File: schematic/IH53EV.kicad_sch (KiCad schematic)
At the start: 43 parts, among them K2 T9AP1D52-12, K3 Cole Hersee 24213, K4 G9EJ-1-E-UVD DC12, SW1 Kill Switch HVBD6AXR, SW3 Ignition Switch, SW4 Inertia Switch

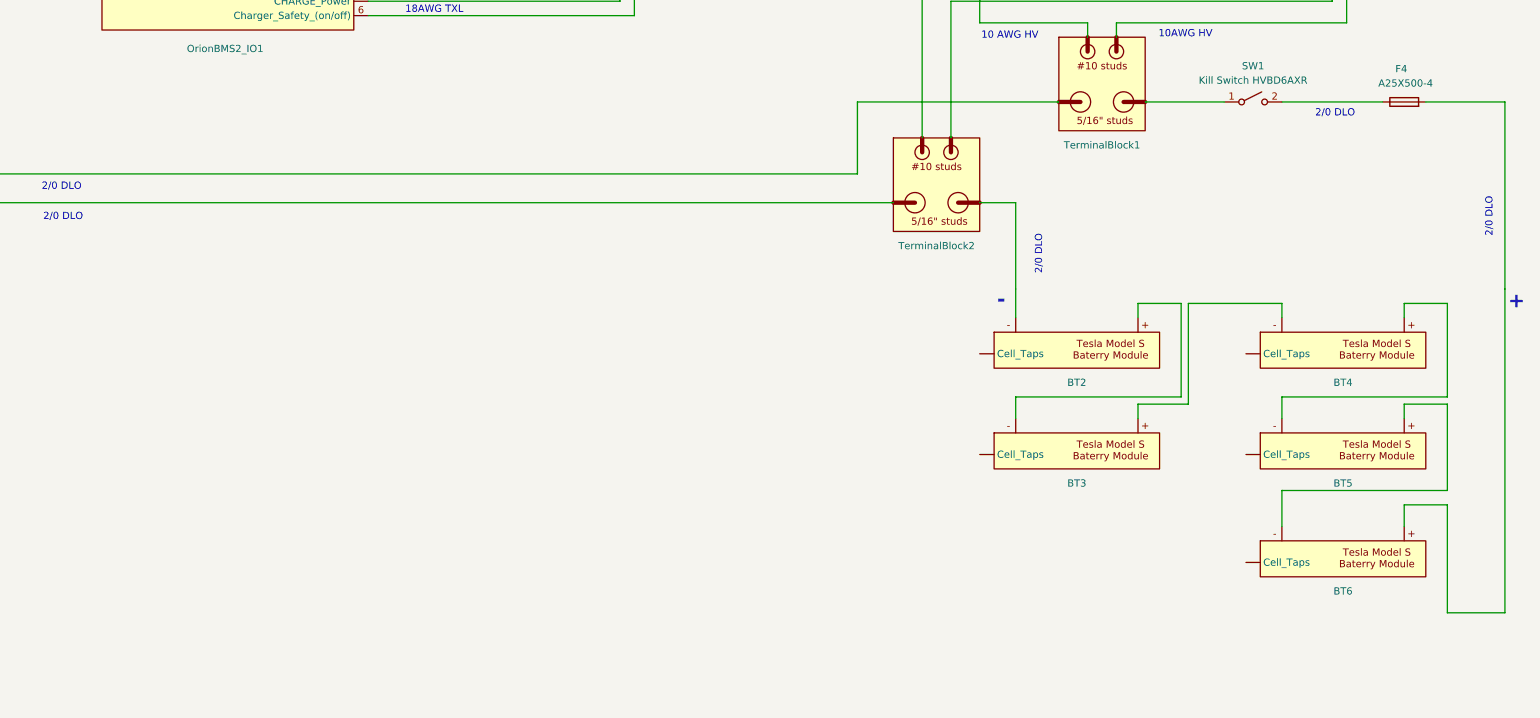
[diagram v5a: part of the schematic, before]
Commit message: add thru-wall terminals
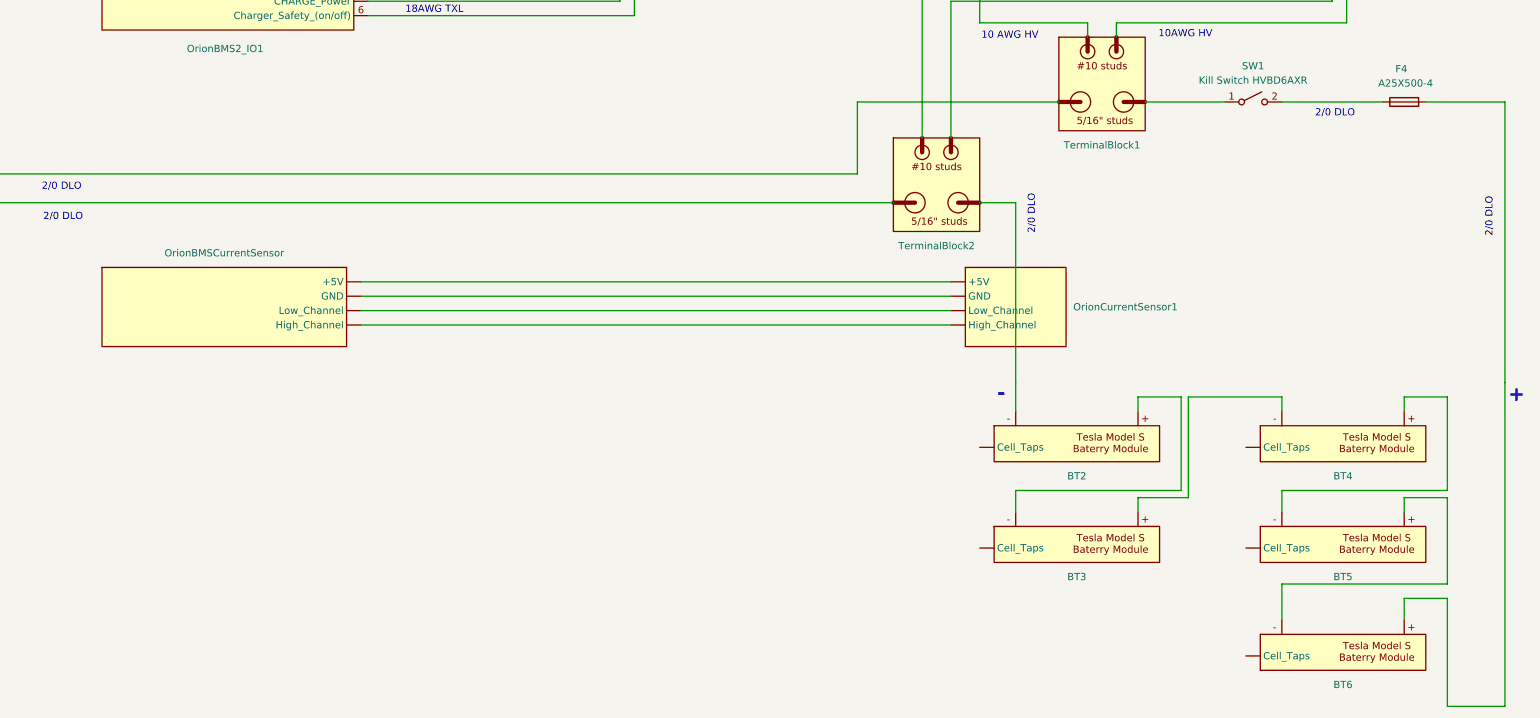
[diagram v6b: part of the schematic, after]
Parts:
- added OrionBMSCurrentSensor: (no value), symbol Orion_BMS:Current_Sensor
- added OrionCurrentSensor1: (no value), symbol Current Sensor:Orion_Current_Sensor
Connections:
- net at DeutschDTM3-pin1.: no longer BBCANOPCanbusIsolator1.
- net at DelphiWeather4Pack1.: now also OrionBMS2_IO1.7 (DISCHARGE_enable); no longer Blue_Sea_5032. (GND)
- net at Blue_Sea_5032.2: no longer DelphiWeather4Pack1.
- net at Blue_Sea_5032.5: now also SW4.2 (B)
- net at BT4.: now also BT3.
- net at BT5.: now also BT6.; no longer BT4.
- net at BT3.: no longer BT4.
- net at NON_ISOLATED_LOGIC_X1_CONTROLLER. (B+): now also G1.A2-; no longer Anderson350A600V1.
- net at BT2.: now also TerminalBlock2.
- net at TerminalBlock2.: now also 2Pole_1000V_DC_10Amp1.2 (B); no longer BT2.
- net at BT6.: no longer BT5.
- net at Anderson350A600V1.: now also TerminalBlock2.; no longer TerminalBlock3.
- net at TerminalBlock1.: now also Circuit_Breaker4.2 (B); no longer Anderson350A600V1.
- net at DCIS_DC/DC_Convertor1. (Key_Switch_Control): now also DJ7021-8-1.; no longer dj70310-6.3-1.
- net at dj70310-6.3-1.: now also 2Pole_1000V_DC_10Amp1.1 (A); no longer DCIS_DC/DC_Convertor1. (Key_Switch_Control)
- net at TerminalBlock3.: now also Circuit_Breaker2.2 (B)
- new net: BBCANOPCanbusIsolator1., DelphiWeather4Pack1., OrionBMS2_IO1.12 (Ground)
- new net: BBCANOPCanbusIsolator1., DeutschDTM3-pin1. (x2)
- new net: OrionBMSCurrentSensor. (High_Channel), OrionCurrentSensor1. (High_Channel) (x4)
- new net: Blue_Sea_5032. (GND), DelphiWeather4Pack1.
- new net: Blue_Sea_5032.2, DelphiWeather4Pack1.
- new net: Blue_Sea_5032.6 (Ready/Precharge), DelphiWeather4Pack1., K2.1
- new net: BT4., BT5.
- new net: Anderson350A600V1., NON_ISOLATED_LOGIC_X1_CONTROLLER. (B+)
- new net: BT2., BT3.
- new net: Anderson350A600V1., TerminalBlock3.
- new net: Anderson350A600V1., TerminalBlock1.
- new net: DCIS_DC/DC_Convertor1. (Key_Switch_Control), dj70310-6.3-1. (x3)
- new net: DCIS_DC/DC_Convertor1. (Key_Switch_Control), DJ7021-8-1.
- now unconnected: BT3., Blue_Sea_5032.6 (Ready/Precharge), DeutschDTM3-pin1.
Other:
- moved on the sheet: BT2, BT3, BT4, BT5, BT6

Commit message: add dashboard
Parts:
- added SW5: Instruments, symbol Switch:SW_SPST
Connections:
- net GND: now also K4.3; no longer K4.1
- net at DeutschDTM3-pin1.: no longer BBCANOPCanbusIsolator1.
- net at DelphiWeather4Pack1.: now also OrionBMS2_IO1.7 (DISCHARGE_enable); no longer Blue_Sea_5032. (GND)
- net at Blue_Sea_5032.2: no longer DelphiWeather4Pack1.
- net at Blue_Sea_5032.4: now also SW5.1 (A)
- net at Blue_Sea_5032.5: now also SW4.2 (B)
- net at BT4.: now also BT3.
- net at BT5.: now also BT6.; no longer BT4.
- net at BT3.: no longer BT4.
- net at NON_ISOLATED_LOGIC_X1_CONTROLLER. (B+): now also G1.A2-; no longer Anderson350A600V1.
- net at K4.4: now also BBCANOPCanbusIsolator1., DelphiWeather4Pack1., OrionBMS2_IO1.2 (READY_Power); no longer dj70310-6.3-1.
- net at BT2.: now also TerminalBlock2.
- net at TerminalBlock2.: now also 2Pole_1000V_DC_10Amp1.2 (B); no longer BT2.
- net at BT6.: no longer BT5.
- net at Anderson350A600V1.: now also TerminalBlock2.; no longer TerminalBlock3.
- net at TerminalBlock1.: now also Circuit_Breaker4.2 (B); no longer Anderson350A600V1.
- net at DCIS_DC/DC_Convertor1. (Key_Switch_Control): now also DJ7021-8-1.; no longer dj70310-6.3-1.
- net at dj70310-6.3-1.: now also 2Pole_1000V_DC_10Amp1.1 (A); no longer DCIS_DC/DC_Convertor1. (Key_Switch_Control)
- net at TerminalBlock3.: now also Circuit_Breaker2.2 (B)
- new net: BBCANOPCanbusIsolator1., DelphiWeather4Pack1., OrionBMS2_IO1.12 (Ground)
- new net: BBCANOPCanbusIsolator1., DeutschDTM3-pin1. (x2)
- new net: OrionBMSCurrentSensor. (High_Channel), OrionCurrentSensor1. (High_Channel) (x3)
- new net: Blue_Sea_5032. (GND), DelphiWeather4Pack1.
- new net: Blue_Sea_5032.2, DelphiWeather4Pack1.
- new net: Blue_Sea_5032.6 (Ready/Precharge), DelphiWeather4Pack1., K2.1
- new net: BT4., BT5.
- new net: Anderson350A600V1., NON_ISOLATED_LOGIC_X1_CONTROLLER. (B+)
- new net: Circuit_Breaker4.1 (A), K4.1, dj70310-6.3-1.
- new net: K4.2, dj70310-6.3-1.
- new net: BT2., BT3.
- new net: Anderson350A600V1., TerminalBlock3.
- new net: Anderson350A600V1., TerminalBlock1.
- new net: DCIS_DC/DC_Convertor1. (Key_Switch_Control), dj70310-6.3-1. (x3)
- new net: DCIS_DC/DC_Convertor1. (Key_Switch_Control), DJ7021-8-1.
- now unconnected: BT3., Blue_Sea_5032.6 (Ready/Precharge), DeutschDTM3-pin1.
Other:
- note added: "to PiCAN 3 +12V (SMPS feeds Pi + TD2)"
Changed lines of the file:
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@@
 	(title_block
 		(title "1953 International EV Conversion")
-		(date "2026-08-24")
+		(date "2026-09-07")
+	)
+	(wire
+		(pts
+			(xy 275.59 218.44) (xy 290.83 218.44)
+		)
+		(stroke
+			(width 0)
+			(type default)
+			(color 0 0 255 1)
+		)
+	)
+	(wire
+		(pts
+			(xy 187.96 125.73) (xy 205.74 125.73)
+		)
+		(stroke
+			(width 0)
+			(type default)
+		)
+	)
+	(wire
+		(pts
+			(xy 215.9 125.73) (xy 233.68 125.73)
+		)
+		(stroke
+			(width 0)
+			(type default)
+		)
+	)
+	(text "to PiCAN 3 +12V\n(SMPS feeds Pi + TD2)"
+		(exclude_from_sim no)
+		(at 248.92 125.73 0)
+		(effects
+			(font
+				(size 1.27 1.27)
+			)
+		)
+	)
+	(text "18AWG TXL"
+		(exclude_from_sim no)
+		(at 196.85 122.0 0)
+		(effects
+			(font
+				(size 1.27 1.27)
+			)
+		)
 	)
 	(text "18AWG TXL"
@@
 	(wire
 		(pts
-			(xy 275.59 218.44) (xy 290.83 218.44)
-		)
-		(stroke
-			(width 0)
-			(type default)
-			(color 0 0 255 1)
-		)
-	)
-	(wire
-		(pts
 			(xy 457.2 151.13) (xy 457.2 77.47)
 		)
@@
 	)
 	(symbol
+		(lib_id "Switch:SW_SPST")
+		(at 210.82 125.73 0)
+		(unit 1)
+		(body_style 1)
+		(exclude_from_sim no)
+		(in_bom yes)
+		(on_board yes)
+		(in_pos_files yes)
+		(dnp no)
+		(fields_autoplaced yes)
+		(property "Reference" "SW5"
+			(at 210.82 118.11 0)
+			(show_name no)
+			(do_not_autoplace no)
+			(effects
+				(font
+					(size 1.27 1.27)
+				)
+			)
+		)
+		(property "Value" "Instruments"
+			(at 210.82 120.65 0)
+			(show_name no)
+			(do_not_autoplace no)
+			(effects
+				(font
+					(size 1.27 1.27)
+				)
+			)
+		)
+		(property "Footprint" ""
+			(at 210.82 125.73 0)
+			(hide yes)
+			(show_name no)
+			(do_not_autoplace no)
+			(effects
+				(font
+					(size 1.27 1.27)
+				)
+			)
+		)
+		(property "Datasheet" ""
+			(at 210.82 125.73 0)
+			(hide yes)
+			(show_name no)
+			(do_not_autoplace no)
+			(effects
+				(font
+					(size 1.27 1.27)
+				)
+			)
+		)
+		(property "Description" "Single Pole Single Throw (SPST) switch"
+			(at 210.82 125.73 0)
+			(hide yes)
+			(show_name no)
+			(do_not_autoplace no)
+			(effects
+				(font
+					(size 1.27 1.27)
+				)
+			)
+		)
+		(pin "1"
+		)
+		(pin "2"
+		)
+		(instances
+			(project "IH53EV"
+				(path "/20bcdb30-6107-4dbd-a268-7abc52ed82ed"
+					(reference "SW5")
+					(unit 1)
+				)
+			)
+		)
+	)
+	(symbol
 		(lib_id "Device:Fuse")
 		(at 90.17 105.41 180)
@@
 	)
 	(symbol
+		(lib_name "Relay_SPST-NO_2")
 		(lib_id "Relay:Relay_SPST-NO")
 		(at 285.75 95.25 90)

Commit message: update bus bar
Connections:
- net at DeutschDTM3-pin1.: no longer BBCANOPCanbusIsolator1.
- net at DelphiWeather4Pack1.: now also OrionBMS2_IO1.7 (DISCHARGE_enable); no longer Blue_Sea_5032. (GND)
- net at Blue_Sea_5032.2: no longer DelphiWeather4Pack1.
- net at Blue_Sea_5032.4: now also SW5.1 (A)
- net at Blue_Sea_5032.5: now also SW4.2 (B)
- net at BT4.: now also BT3.
- net at BT5.: now also BT6.; no longer BT4.
- net at BT3.: no longer BT4.
- net at NON_ISOLATED_LOGIC_X1_CONTROLLER. (B+): now also G1.A2-; no longer Anderson350A600V1.
- net at BT2.: now also TerminalBlock2.
- net at TerminalBlock2.: now also 2Pole_1000V_DC_10Amp1.2 (B); no longer BT2.
- net at BT6.: no longer BT5.
- net at Anderson350A600V1.: now also TerminalBlock2.; no longer TerminalBlock3.
- net at TerminalBlock1.: now also Circuit_Breaker4.2 (B); no longer Anderson350A600V1.
- net at DCIS_DC/DC_Convertor1. (Key_Switch_Control): now also DJ7021-8-1.; no longer dj70310-6.3-1.
- net at dj70310-6.3-1.: now also 2Pole_1000V_DC_10Amp1.1 (A); no longer DCIS_DC/DC_Convertor1. (Key_Switch_Control)
- net at TerminalBlock3.: now also Circuit_Breaker2.2 (B)
- new net: BBCANOPCanbusIsolator1., DelphiWeather4Pack1., OrionBMS2_IO1.12 (Ground)
- new net: BBCANOPCanbusIsolator1., DeutschDTM3-pin1. (x2)
- new net: OrionBMSCurrentSensor. (High_Channel), OrionCurrentSensor1. (High_Channel) (x3)
- new net: Blue_Sea_5032. (GND), DelphiWeather4Pack1.
- new net: Blue_Sea_5032.2, DelphiWeather4Pack1.
- new net: Blue_Sea_5032.6 (Ready/Precharge), DelphiWeather4Pack1., K2.1
- new net: BT4., BT5.
- new net: Anderson350A600V1., NON_ISOLATED_LOGIC_X1_CONTROLLER. (B+)
- new net: BT2., BT3.
- new net: Anderson350A600V1., TerminalBlock3.
- new net: Anderson350A600V1., TerminalBlock1.
- new net: DCIS_DC/DC_Convertor1. (Key_Switch_Control), dj70310-6.3-1. (x3)
- new net: DCIS_DC/DC_Convertor1. (Key_Switch_Control), DJ7021-8-1.
- now unconnected: BT3., Blue_Sea_5032.6 (Ready/Precharge), DeutschDTM3-pin1.
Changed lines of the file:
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@@
 		(date "2026-09-07")
 	)
-	(wire
-		(pts
-			(xy 275.59 218.44) (xy 290.83 218.44)
-		)
-		(stroke
-			(width 0)
-			(type default)
-			(color 0 0 255 1)
-		)
-	)
-	(wire
-		(pts
-			(xy 187.96 125.73) (xy 205.74 125.73)
-		)
-		(stroke
-			(width 0)
-			(type default)
-		)
-	)
-	(wire
-		(pts
-			(xy 215.9 125.73) (xy 233.68 125.73)
-		)
-		(stroke
-			(width 0)
-			(type default)
-		)
-	)
-	(text "to PiCAN 3 +12V\n(SMPS feeds Pi + TD2)"
-		(exclude_from_sim no)
-		(at 248.92 125.73 0)
-		(effects
-			(font
-				(size 1.27 1.27)
-			)
-		)
-	)
-	(text "18AWG TXL"
-		(exclude_from_sim no)
-		(at 196.85 122.0 0)
-		(effects
-			(font
-				(size 1.27 1.27)
-			)
-		)
-	)
 	(text "18AWG TXL"
 		(exclude_from_sim no)
@@
 		)
 	)
+	(text "18AWG TXL"
+		(exclude_from_sim no)
+		(at 196.85 122 0)
+		(effects
+			(font
+				(size 1.27 1.27)
+			)
+		)
+	)
 	(text "Vehicle Front"
 		(exclude_from_sim no)
@@
 		)
 	)
+	(text "to PiCAN 3 +12V\n(SMPS feeds Pi + TD2)"
+		(exclude_from_sim no)
+		(at 248.92 125.73 0)
+		(effects
+			(font
+				(size 1.27 1.27)
+			)
+		)
+	)
 	(text "18AWG TXL"
 		(exclude_from_sim no)
@@
 		)
 	)
+	(wire
+		(pts
+			(xy 215.9 125.73) (xy 233.68 125.73)
+		)
+		(stroke
+			(width 0)
+			(type default)
+		)
+	)
 	(polyline
 		(pts
@@
 	(wire
 		(pts
+			(xy 187.96 125.73) (xy 205.74 125.73)
+		)
+		(stroke
+			(width 0)
+			(type default)
+		)
+	)
+	(wire
+		(pts
 			(xy 483.87 311.15) (xy 476.25 311.15)
 		)
@@
 	(wire
 		(pts
+			(xy 275.59 218.44) (xy 290.83 218.44)
+		)
+		(stroke
+			(width 0)
+			(type default)
+			(color 0 0 255 1)
+		)
+	)
+	(wire
+		(pts
 			(xy 457.2 151.13) (xy 457.2 77.47)
 		)
@@
 	)
 	(symbol
-		(lib_id "Switch:SW_SPST")
-		(at 210.82 125.73 0)
-		(unit 1)
-		(body_style 1)
-		(exclude_from_sim no)
-		(in_bom yes)
-		(on_board yes)
-		(in_pos_files yes)
-		(dnp no)
-		(fields_autoplaced yes)
-		(property "Reference" "SW5"
-			(at 210.82 118.11 0)
-			(show_name no)
-			(do_not_autoplace no)
-			(effects
-				(font
-					(size 1.27 1.27)
-				)
-			)
-		)
-		(property "Value" "Instruments"
-			(at 210.82 120.65 0)
-			(show_name no)
-			(do_not_autoplace no)
-			(effects
-				(font
-					(size 1.27 1.27)
-				)
-			)
-		)
-		(property "Footprint" ""
-			(at 210.82 125.73 0)
-			(hide yes)
-			(show_name no)
-			(do_not_autoplace no)
-			(effects
-				(font
-					(size 1.27 1.27)
-				)
-			)
-		)
-		(property "Datasheet" ""
-			(at 210.82 125.73 0)
-			(hide yes)
-			(show_name no)
-			(do_not_autoplace no)
-			(effects
-				(font
-					(size 1.27 1.27)
-				)
-			)
-		)
-		(property "Description" "Single Pole Single Throw (SPST) switch"
-			(at 210.82 125.73 0)
-			(hide yes)
-			(show_name no)
-			(do_not_autoplace no)
-			(effects
-				(font
-					(size 1.27 1.27)
-				)
-			)
-		)
-		(pin "1"
-		)
-		(pin "2"
-		)
-		(instances
-			(project "IH53EV"
-				(path "/20bcdb30-6107-4dbd-a268-7abc52ed82ed"
-					(reference "SW5")
-					(unit 1)
-				)
-			)
-		)
-	)
-	(symbol
 		(lib_id "Device:Fuse")
 		(at 90.17 105.41 180)
@@
 					(unit 1)
 				)
+			)
+		)
+	)
+	(symbol
+		(lib_id "Switch:SW_SPST")
+		(at 210.82 125.73 0)
+		(unit 1)
+		(body_style 1)
+		(exclude_from_sim no)
+		(in_bom yes)
+		(on_board yes)
+		(in_pos_files yes)
+		(dnp no)
+		(fields_autoplaced yes)
+		(property "Reference" "SW5"
+			(at 210.82 118.11 0)
+			(show_name no)
+			(do_not_autoplace no)
+			(effects
+				(font
+					(size 1.27 1.27)
+				)
+			)
+		)
+		(property "Value" "Instruments"
+			(at 210.82 120.65 0)
+			(show_name no)
+			(do_not_autoplace no)
+			(effects
+				(font
+					(size 1.27 1.27)
+				)
+			)
+		)
+		(property "Footprint" ""
+			(at 210.82 125.73 0)
+			(hide yes)
+			(show_name no)
+			(do_not_autoplace no)
+			(effects
+				(font
+					(size 1.27 1.27)
+				)
+			)
+		)
+		(property "Datasheet" ""
+			(at 210.82 125.73 0)
+			(hide yes)
+			(show_name no)
+			(do_not_autoplace no)
+			(effects
+				(font
+					(size 1.27 1.27)
+				)
+			)
+		)
+		(property "Description" "Single Pole Single Throw (SPST) switch"
+			(at 210.82 125.73 0)
+			(hide yes)
+			(show_name no)
+			(do_not_autoplace no)
+			(effects
+				(font
+					(size 1.27 1.27)
+				)
+			)
+		)
+		(pin "1"
+		)
+		(pin "2"
+		)
+		(instances
+			(project "IH53EV"
+				(path "/20bcdb30-6107-4dbd-a268-7abc52ed82ed"
+					(reference "SW5")
+					(unit 1)
+				)
